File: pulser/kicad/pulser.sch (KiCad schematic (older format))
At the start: 46 parts, among them J1 Screw_Terminal_01x02, J2 Screw_Terminal_01x02, J3 Conn_01x06_Male, J4 Screw_Terminal_01x02, J5 Conn_01x07_Male, Q1 RQ6E080AJTCR, Q2 RQ6E080AJTCR, SW1 SW_Push, SW2 SW_Push, SW3 SW_Push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

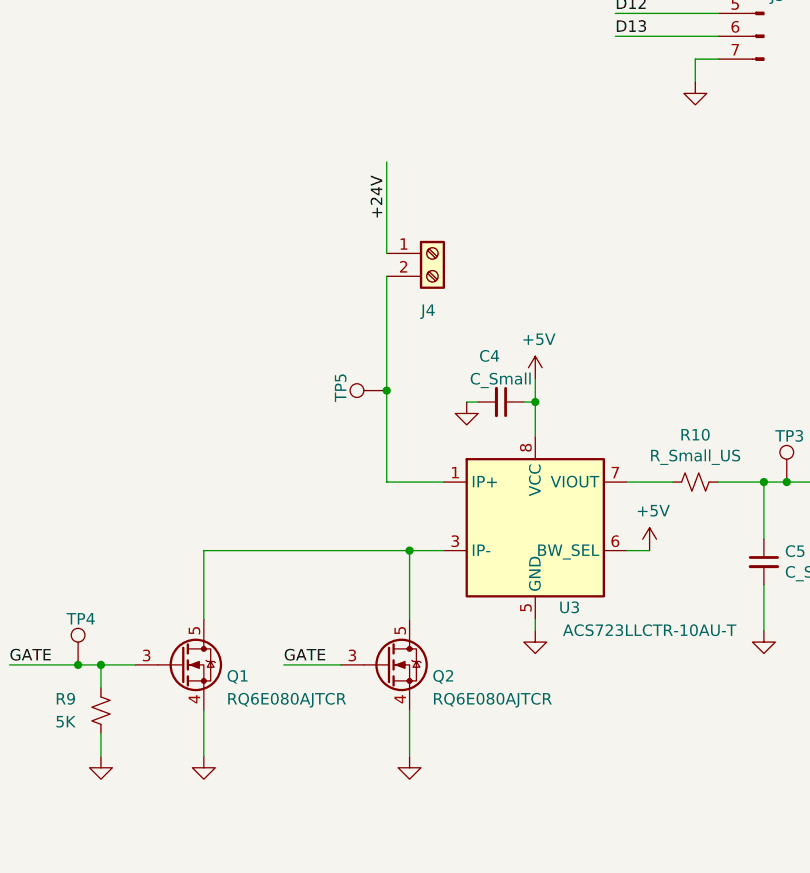
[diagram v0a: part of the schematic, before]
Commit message: Cleaned up and generted ground plane.
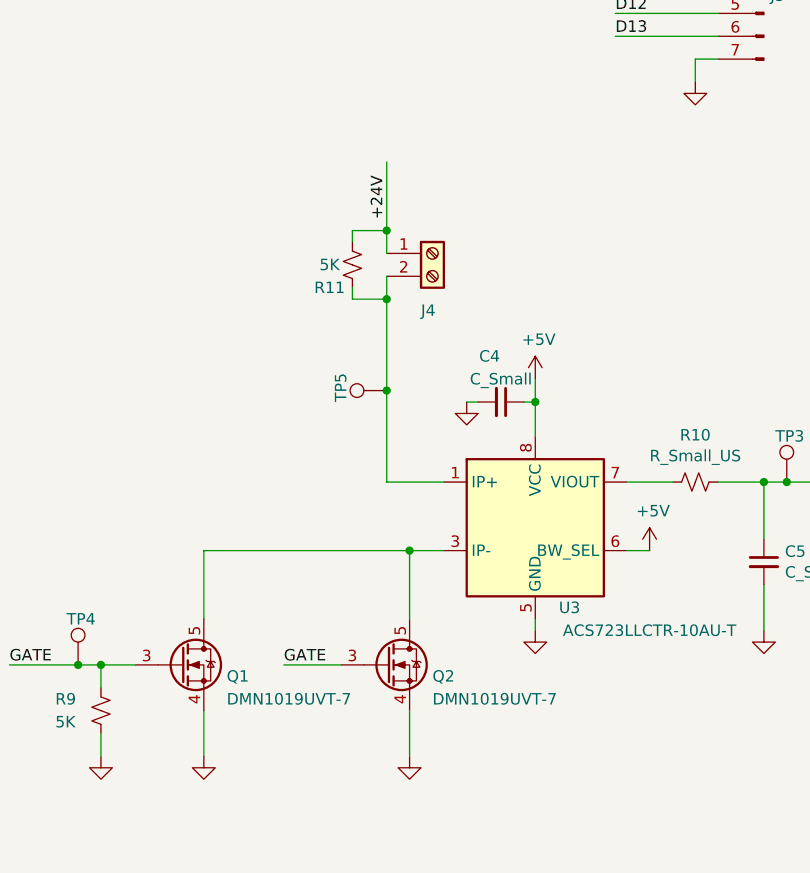
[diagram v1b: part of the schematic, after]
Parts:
- added R11: 5K, Resistor_SMD:R_0603_1608Metric, symbol Device:R_Small_US
- C2: footprint Capacitor_THT:CP_Radial_D8.0mm_P2.50mm -> pulsar:CP_Radial_D8.0mm_P2.50mm
- C3: footprint Capacitor_THT:CP_Radial_D5.0mm_P2.00mm -> pulsar:CP_Radial_D5.0mm_P2.00mm
- Q1, Q2: value RQ6E080AJTCR -> DMN1019UVT-7
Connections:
- wire segments 138 -> 144
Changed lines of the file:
@@
 P 7050 5700
 F 0 "Q1" H 7250 5650 50  0000 L CNN
-F 1 "RQ6E080AJTCR" H 7250 5550 50  0000 L CNN
+F 1 "DMN1019UVT-7" H 7250 5550 50  0000 L CNN
 F 2 "Package_TO_SOT_SMD:SOT-23-6_Handsoldering" H 7250 5625 50  0001 L CIN
 F 3 "https://assets.nexperia.com/documents/data-sheet/BUK9M24-60E.pdf" V 7050 5700 50  0001 L CNN
@@
 F 0 "C3" H 4050 2150 50  0000 L CNN
 F 1 "22u 10V" H 4050 2000 50  0000 L CNN
-F 2 "Capacitor_THT:CP_Radial_D5.0mm_P2.00mm" H 3850 2100 50  0001 C CNN
+F 2 "pulsar:CP_Radial_D5.0mm_P2.00mm" H 3850 2100 50  0001 C CNN
 F 3 "~" H 3850 2100 50  0001 C CNN
 	1    3850 2100
@@
 F 0 "C2" H 2450 2200 50  0000 L CNN
 F 1 "10u 50V" H 2200 2100 50  0000 L CNN
-F 2 "Capacitor_THT:CP_Radial_D8.0mm_P2.50mm" H 2700 2100 50  0001 C CNN
+F 2 "pulsar:CP_Radial_D8.0mm_P2.50mm" H 2700 2100 50  0001 C CNN
 F 3 "~" H 2700 2100 50  0001 C CNN
 	1    2700 2100
@@
 P 7950 5700
 F 0 "Q2" H 8150 5650 50  0000 L CNN
-F 1 "RQ6E080AJTCR" H 8150 5550 50  0000 L CNN
+F 1 "DMN1019UVT-7" H 8150 5550 50  0000 L CNN
 F 2 "Package_TO_SOT_SMD:SOT-23-6_Handsoldering" H 8150 5625 50  0001 L CIN
 F 3 "https://assets.nexperia.com/documents/data-sheet/BUK9M24-60E.pdf" V 7950 5700 50  0001 L CNN
@@
 	6600 5700 6300 5700
 Wire Wire Line
-	7950 4000 7950 4500
+	7950 4000 7950 4100
 Connection ~ 7950 4500
 Wire Wire Line
@@
 $EndComp
 Wire Wire Line
-	7950 3500 7950 3900
+	7950 3500 7950 3800
 Text Label 7950 3750 1    50   ~ 0
 +24V
@@
 	1    0    0    -1
 $EndComp
+$Comp
+L Device:R_Small_US R11
+U 1 1 5FA43B79
+P 7800 3950
+F 0 "R11" H 7900 4050 50  0000 C CNN
+F 1 "5K" H 7900 3950 50  0000 C CNN
+F 2 "Resistor_SMD:R_0603_1608Metric" H 7800 3950 50  0001 C CNN
+F 3 "~" H 7800 3950 50  0001 C CNN
+	1    7800 3950
+	-1   0    0    1
+$EndComp
+Wire Wire Line
+	7800 3850 7800 3800
+Wire Wire Line
+	7800 3800 7950 3800
+Connection ~ 7950 3800
+Wire Wire Line
+	7950 3800 7950 3900
+Wire Wire Line
+	7800 4050 7800 4100
+Wire Wire Line
+	7800 4100 7950 4100
+Connection ~ 7950 4100
+Wire Wire Line
+	7950 4100 7950 4500
 $EndSCHEMATC

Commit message: Left over from previous commit.
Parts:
- D1: value S10ML-TP -> SB2060TA
- D3, D5: value Z3SMCxxx -> MBRX120LF-TP
- J2, J4: footprint TerminalBlock:TerminalBlock_bornier-2_P5.08mm -> pulsar:TerminalBlock_bornier-2_P5.08mm
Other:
- note removed: "TODO: test gate driving speed"
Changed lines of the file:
@@
 F 0 "J4" H 8100 3650 50  0000 L CNN
 F 1 "Screw_Terminal_01x02" H 8230 3801 50  0001 L CNN
-F 2 "TerminalBlock:TerminalBlock_bornier-2_P5.08mm" H 8150 3900 50  0001 C CNN
+F 2 "pulsar:TerminalBlock_bornier-2_P5.08mm" H 8150 3900 50  0001 C CNN
 F 3 "~" H 8150 3900 50  0001 C CNN
 	1    8150 3900
@@
 F 0 "J2" H 1650 1050 50  0000 C CNN
 F 1 "Screw_Terminal_01x02" H 1568 1426 50  0001 C CNN
-F 2 "TerminalBlock:TerminalBlock_bornier-2_P5.08mm" H 1650 1300 50  0001 C CNN
+F 2 "pulsar:TerminalBlock_bornier-2_P5.08mm" H 1650 1300 50  0001 C CNN
 F 3 "~" H 1650 1300 50  0001 C CNN
 	1    1650 1300
@@
 P 2400 1300
 F 0 "D1" H 2250 1400 50  0000 C CNN
-F 1 "S10ML-TP" H 2400 1500 50  0000 C CNN
+F 1 "SB2060TA" H 2400 1500 50  0000 C CNN
 F 2 "Diode_THT:D_DO-201AD_P12.70mm_Horizontal" H 2400 1125 50  0001 C CNN
 F 3 "https://diotec.com/tl_files/diotec/files/pdf/datasheets/z3smc1.pdf" H 2400 1300 50  0001 C CNN
@@
 P 3950 3400
 F 0 "D5" V 3996 3320 50  0000 R CNN
-F 1 "Z3SMCxxx" V 3905 3320 50  0000 R CNN
+F 1 "MBRX120LF-TP" V 3905 3320 50  0000 R CNN
 F 2 "Diode_SMD:D_SOD-123" H 3950 3225 50  0001 C CNN
 F 3 "https://diotec.com/tl_files/diotec/files/pdf/datasheets/z3smc1.pdf" H 3950 3400 50  0001 C CNN
@@
 P 3550 4300
 F 0 "D3" H 3700 4350 50  0000 C CNN
-F 1 "Z3SMCxxx" H 3300 4350 50  0000 C CNN
+F 1 "MBRX120LF-TP" H 3300 4350 50  0000 C CNN
 F 2 "Diode_SMD:D_SOD-123" H 3550 4125 50  0001 C CNN
 F 3 "https://diotec.com/tl_files/diotec/files/pdf/datasheets/z3smc1.pdf" H 3550 4300 50  0001 C CNN
@@
 Text Label 7500 5700 0    50   ~ 0
 GATE
-Text Notes 950  3050 0    79   ~ 0
-TODO: test gate driving speed
 Wire Wire Line
 	5650 4750 5650 5100

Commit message: Narrower fuse slot. Also regenerated gerbers.
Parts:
- F1: footprint Fuse:Fuse_Blade_Mini_directSolder -> pulsar:Fuse_Blade_Mini_directSolder
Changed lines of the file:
@@
 F 0 "F1" H 2050 1485 50  0000 C CNN
 F 1 "10A" H 2050 1394 50  0000 C CNN
-F 2 "Fuse:Fuse_Blade_Mini_directSolder" H 2050 1300 50  0001 C CNN
+F 2 "pulsar:Fuse_Blade_Mini_directSolder" H 2050 1300 50  0001 C CNN
 F 3 "~" H 2050 1300 50  0001 C CNN
 	1    2050 1300
